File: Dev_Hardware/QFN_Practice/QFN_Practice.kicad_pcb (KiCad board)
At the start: 2 copper layers, 32 parts, among them J1 USB_C_Receptacle_USB2.0_16P, J2 FTSH-105-01-X-DV-K-X, J3 Conn_01x14_Pin, J4 Conn_01x14_Pin, SW1 SW_Push, SW3 SW_Push, U1 LPC824M201JHI33, U2 CP2102N-Axx-xQFN20, U3 XC6206PxxxMR

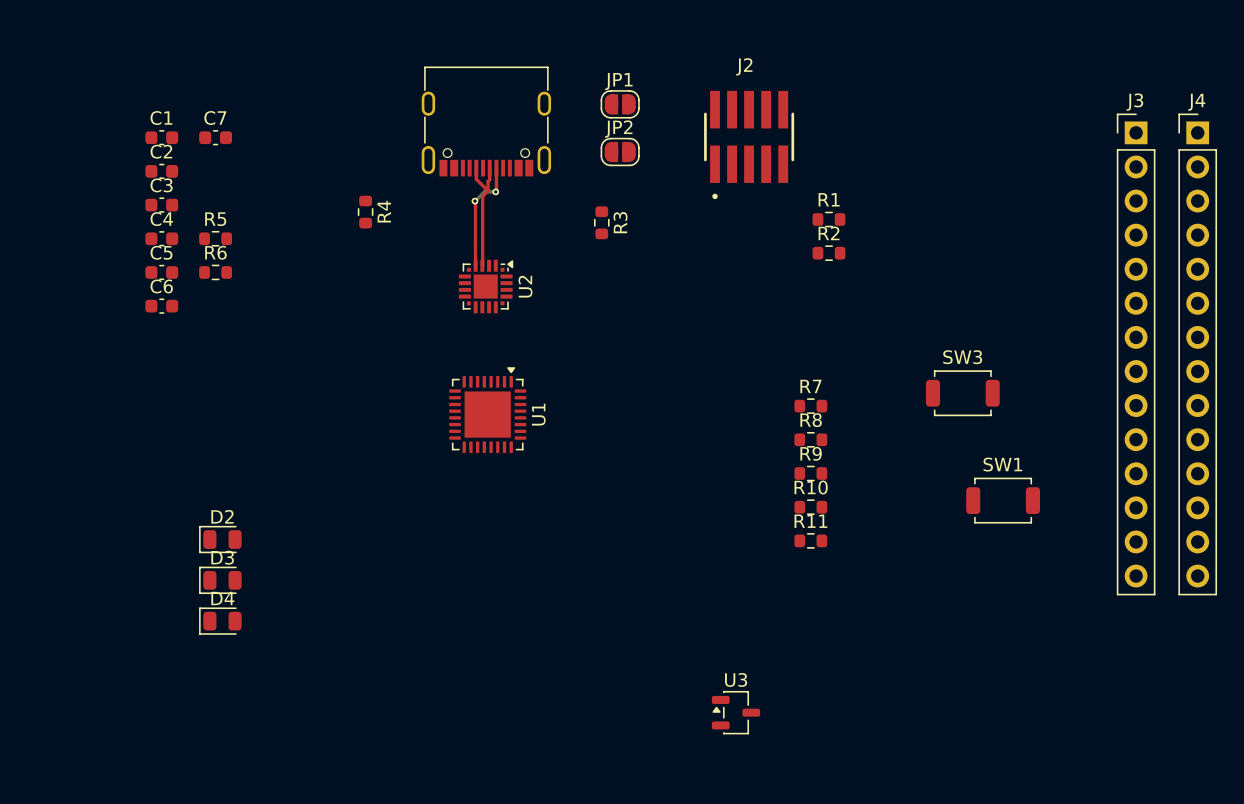
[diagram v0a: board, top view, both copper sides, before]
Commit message: finished routing for all but power regulation and GPIO
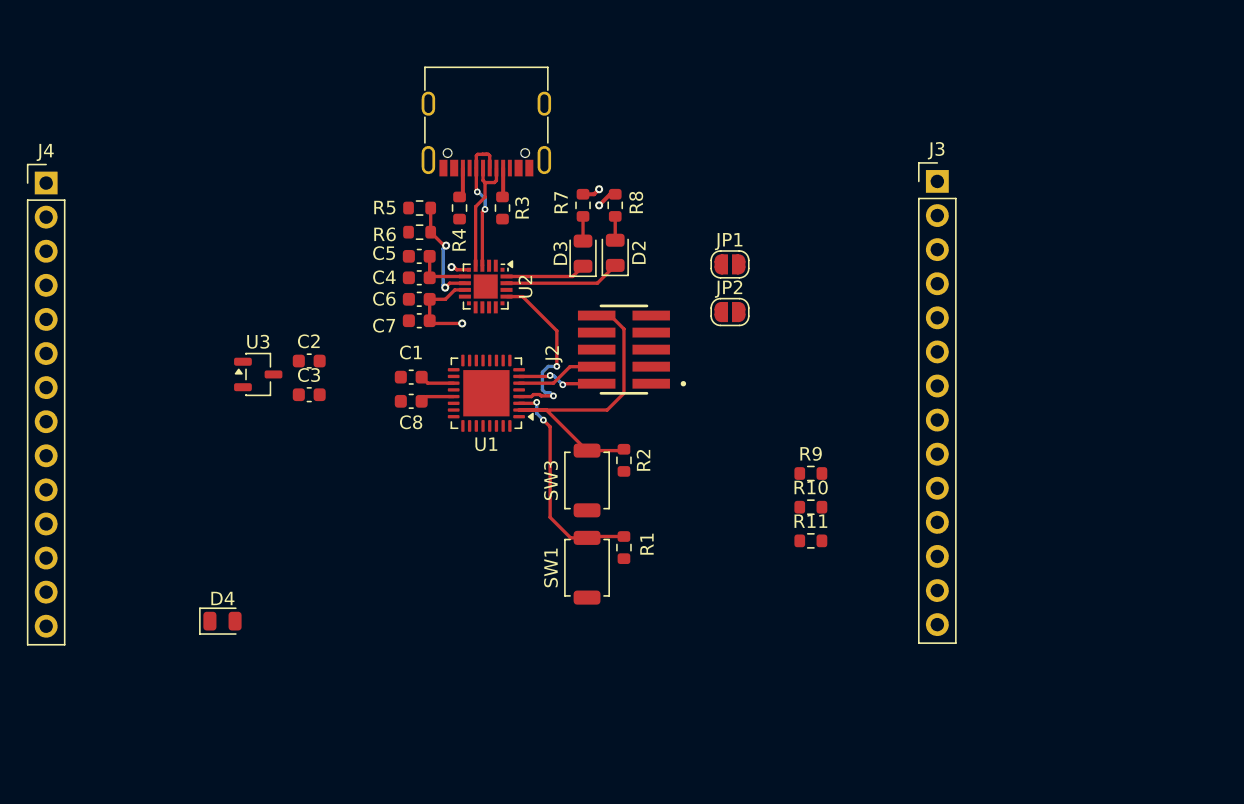
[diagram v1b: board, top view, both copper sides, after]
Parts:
- added C8: 100nf, Capacitor_SMD:C_0603_1608Metric, F.Cu at (47.4, 66.6)
- moved J4 85.9 mm to (20.2, 50.3)
- moved U3 43.6 mm to (36.0, 64.6)
- moved D3 36.2 mm to (60.2, 55.6), turned to 90 degrees
- moved D2 36.2 mm to (62.6, 55.5), turned to 90 degrees
- moved SW1 31.4 mm to (60.5, 79.0), turned to 90 degrees
- moved R1 28.8 mm to (63.2, 77.5), turned to 90 degrees
- moved SW3 28.7 mm to (60.5, 72.5), turned to 90 degrees
- moved C1 25.8 mm to (47.4, 64.8), turned to 180 degrees
- moved R8 22.8 mm to (62.6, 52.0), turned to -90 degrees
- moved R7 22.6 mm to (60.2, 52.0), turned to -90 degrees
- moved R2 21.7 mm to (63.2, 71.0), turned to 90 degrees
- moved C7 20.4 mm to (48.0, 60.6), turned to 180 degrees
- moved C4 19.4 mm to (48.0, 57.4), turned to 180 degrees
- moved C5 19.2 mm to (48.0, 55.8), turned to 180 degrees
- moved C6 19.2 mm to (48.0, 59.0), turned to 180 degrees
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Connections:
- J2 pad 02: /MCU_Support/m_SWCLK -> /SWCLK
- J2 pad 04: /MCU_Support/m_SWDIO -> /SWDIO
- J2 pad 10: /MCU_Support/nRST -> /nRST
- R1 pad 2: /MCU_Support/ISP -> /ISP
- R2 pad 2: /MCU_Support/nRST -> /nRST
- SW1 pad 2: /MCU_Support/ISP -> /ISP
- SW3 pad 2: /MCU_Support/nRST -> /nRST
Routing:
- net /nRST: track 0.00 -> 24.7 mm
- net /ISP: track 0.00 -> 16.5 mm, vias 0 -> 2
- net /TXD_MCU: track 0.00 -> 13.7 mm, vias 0 -> 2
- net /3v3_CP: track 0.00 -> 11.3 mm, vias 0 -> 4
- net Net-(D2-K): track 0.00 -> 8.65 mm
- net /VBUS_CP: track 0.00 -> 8.26 mm, vias 0 -> 2
- net /SWDIO: track 0.00 -> 6.29 mm
- net /SWCLK: track 0.00 -> 6.13 mm, vias 0 -> 2
- net Net-(D3-K): track 0.00 -> 6.02 mm
- net +3V3: track 0.00 -> 5.11 mm
- net +5V: track 0.00 -> 4.27 mm
- net Net-(J1-CC2): track 0.00 -> 2.25 mm
- net Net-(J1-CC1): track 0.00 -> 2.17 mm
- net Net-(D3-A): track 0.00 -> 1.84 mm
- net Net-(D2-A): track 0.00 -> 1.77 mm
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- added copper zone on In2.Cu, net /3v3_CP
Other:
- copper layers 2 -> 4

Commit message: finished layout
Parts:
- moved J4 50.9 mm to (71.1, 50.3)
- moved J3 46.0 mm to (40.6, 50.2)
- moved D4 25.8 mm to (56.2, 71.0), turned to 90 degrees
- moved R9 21.1 mm to (56.2, 74.4), turned to -90 degrees
- moved JP2 20.5 mm to (66.6, 80.0), turned to -90 degrees
- moved JP1 18.6 mm to (66.6, 74.4), turned to -90 degrees
- moved R10 11.6 mm to (66.2, 70.8), turned to 90 degrees
- moved U3 11.3 mm to (45.4, 70.8), turned to 180 degrees
- moved R11 11.2 mm to (67.8, 70.8), turned to 90 degrees
- moved C2 10.4 mm to (43.4, 73.4), turned to -90 degrees
- moved C3 9.80 mm to (48.4, 70.8), turned to -90 degrees
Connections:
- R11 pad 2: /SDA -> /SCL
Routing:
- net /SCL: track 0.00 -> 25.4 mm, vias 0 -> 4
- net /SDA: track 0.00 -> 22.2 mm, vias 0 -> 2
- net Net-(JP2-A): track 0.00 -> 8.17 mm
- net Net-(JP1-A): track 0.00 -> 2.29 mm
- net /nRST: track 24.7 -> 22.5 mm
- added copper zone on In2.Cu, net +5V
- added copper zone on In1.Cu, net GND
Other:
- board outline added: 35.5 x 42.5 mm

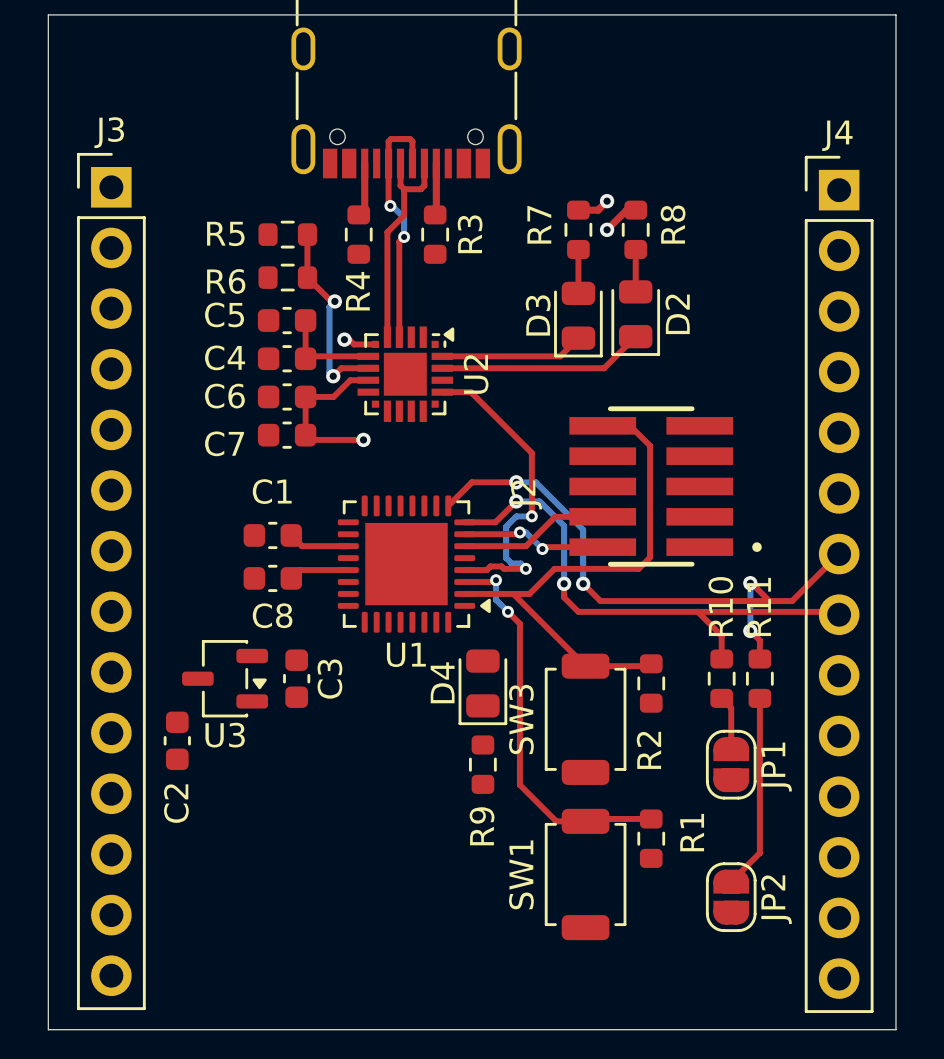
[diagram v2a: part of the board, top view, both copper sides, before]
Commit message: routed more of the QFN test pcb
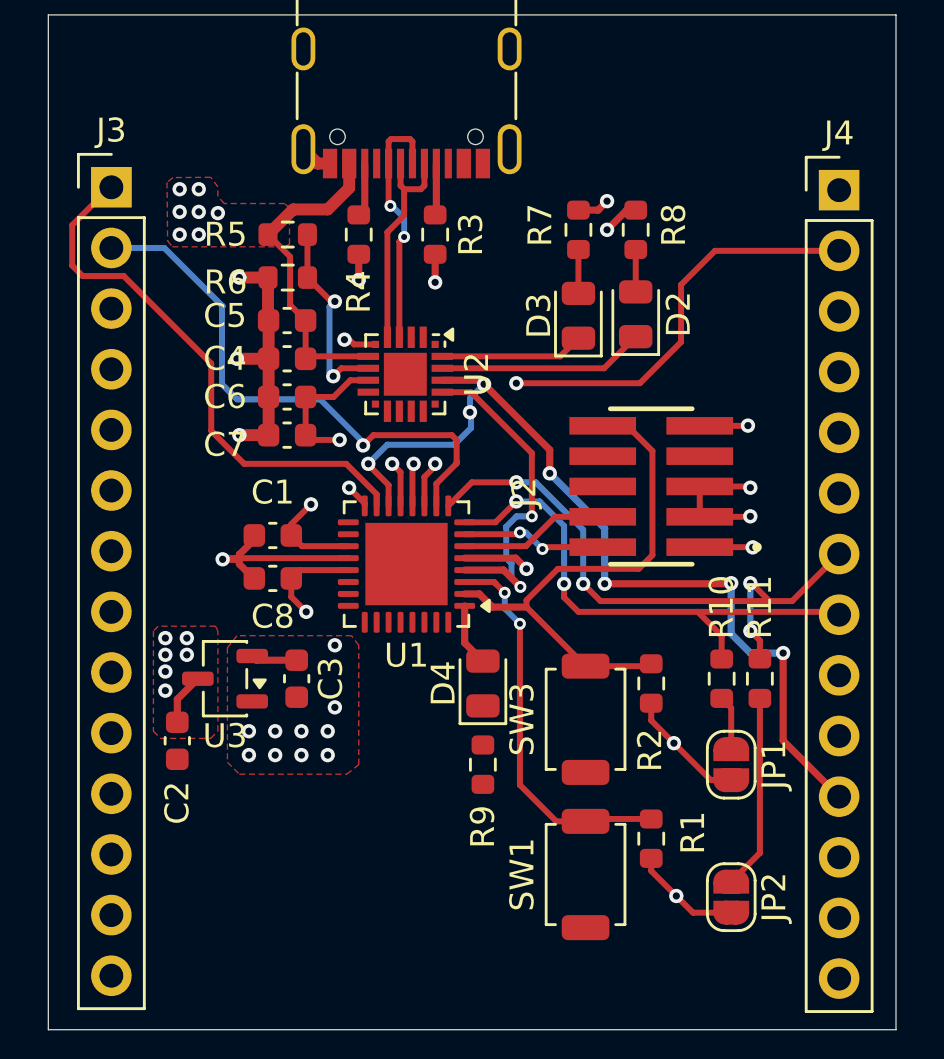
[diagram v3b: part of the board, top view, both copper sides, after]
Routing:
- net /RXD_MCU: track 0.00 -> 38.4 mm, vias 0 -> 7
- net GND: track 0.00 -> 29.9 mm, vias 0 -> 9
- net Net-(J3-Pin_2): track 0.00 -> 23.3 mm, vias 0 -> 1
- net Net-(J3-Pin_1): track 0.00 -> 22.9 mm
- net /P2: track 0.00 -> 18.3 mm, vias 0 -> 2
- net +3V3: track 5.11 -> 22.3 mm, vias 0 -> 15
- net +5V: track 4.27 -> 15.9 mm, vias 0 -> 13
- net Net-(J3-Pin_14): track 0.00 -> 2.77 mm, vias 0 -> 1
- net Net-(D4-A): track 0.00 -> 2.63 mm
- net Net-(J3-Pin_13): track 0.00 -> 1.95 mm, vias 0 -> 1
- net Net-(J3-Pin_11): track 0.00 -> 1.91 mm, vias 0 -> 1
- net Net-(J3-Pin_12): track 0.00 -> 1.78 mm, vias 0 -> 1
- net /3v3_CP: track 11.3 -> 10.3 mm
- added copper zone on F.Cu, net +3V3
- added copper zone on In2.Cu, net +3V3
- added copper zone on F.Cu, net +5V

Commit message: finished layout and routing
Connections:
- net Net-(J3-Pin_1) renamed /P15
- net Net-(J3-Pin_11) renamed /P25
- net Net-(J3-Pin_12) renamed /P26
- net Net-(J3-Pin_13) renamed /P27
- net Net-(J3-Pin_14) renamed /P28
- net Net-(J3-Pin_2) renamed /P16
- net Net-(J3-Pin_9) renamed /P23
- J3 pad 10: unconnected-(J3-Pin_10-Pad10) -> /P22
- J3 pad 3: Net-(J3-Pin_3) -> /P9
- J3 pad 4: Net-(J3-Pin_4) -> /P8
- J3 pad 5: Net-(J3-Pin_5) -> /P7
- J3 pad 6: Net-(J3-Pin_6) -> /P6
- J3 pad 7: Net-(J3-Pin_7) -> /P1
- J3 pad 8: Net-(J3-Pin_8) -> /P14
- J4 pad 1: /P1 -> +5V
- J4 pad 12: +5V -> /P19
- J4 pad 13: GND -> /P20
- J4 pad 14: GND -> /P21
- J4 pad 2: /P2 -> GND
- J4 pad 3: /P6 -> GND
- J4 pad 4: /P7 -> /P2
- J4 pad 5: /P8 -> unconnected-(J4-Pin_5-Pad5)
- J4 pad 6: /P9 -> /P17
- J4 pad 9: /P14 -> /P18
- U1 pad 27: Net-(J3-Pin_8) -> /P22
- U1 pad 28: Net-(J3-Pin_7) -> /P21
- U1 pad 29: Net-(J3-Pin_6) -> /P20
- U1 pad 30: Net-(J3-Pin_5) -> /P19
- U1 pad 31: Net-(J3-Pin_4) -> /P18
- U1 pad 32: Net-(J3-Pin_3) -> /P17
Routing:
- net /P28: track 2.77 -> 33.3 mm, vias 1 -> 2
- net /P21: track 0.00 -> 30.1 mm, vias 0 -> 2
- net /P20: track 0.00 -> 29.6 mm, vias 0 -> 2
- net /P19: track 0.00 -> 29.2 mm, vias 0 -> 2
- net /P27: track 1.95 -> 30.9 mm, vias 1 -> 2
- net /P26: track 1.78 -> 28.4 mm, vias 1 -> 2
- net GND: track 29.9 -> 55.7 mm, vias 9 -> 73
- net /P25: track 1.91 -> 27.7 mm, vias 1 -> 2
- net /P18: track 0.00 -> 22.0 mm, vias 0 -> 2
- net /P17: track 0.00 -> 19.9 mm, vias 0 -> 2
- net /TXD_MCU: track 14.1 -> 33.1 mm, vias 2 -> 4
- net /P22: track 0.00 -> 18.7 mm
- net /3v3_CP: track 10.3 -> 26.8 mm
- net /P7: track 0.00 -> 15.6 mm, vias 0 -> 2
- net /P9: track 0.00 -> 15.3 mm
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- added copper zone on F.Cu, net GND
